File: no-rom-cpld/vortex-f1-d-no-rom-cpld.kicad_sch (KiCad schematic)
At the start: 50 parts, among them J1 JTAG, J2 CONFIG, U1 FDC 9229, U2 XC9572XL, U3 AZ1117-3.3, U4 uPD765AC, U5 74LS06N, U6 74LS06N, U7 SN74LS07N, X1 8Mhz

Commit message: cpl wip
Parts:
- removed C5, C6, C7, C8, C9: 100n, Capacitor_SMD:C_0603_1608Metric_Pad1.08x0.95mm_HandSolder, symbol Device:C_Small
- removed J2: CONFIG, Connector_PinHeader_2.54mm:PinHeader_2x04_P2.54mm_Vertical, symbol Connector_Generic:Conn_02x04_Odd_Even
- removed LED1: LED1, LED_SMD:LED_0805_2012Metric_Pad1.15x1.40mm_HandSolder, symbol Device:LED_Small_Filled
- removed LED2: LED2, LED_SMD:LED_0805_2012Metric_Pad1.15x1.40mm_HandSolder, symbol Device:LED_Small_Filled
- removed LED3: LED3, LED_SMD:LED_0805_2012Metric_Pad1.15x1.40mm_HandSolder, symbol Device:LED_Small_Filled
- removed LED4: LED4, LED_SMD:LED_0805_2012Metric_Pad1.15x1.40mm_HandSolder, symbol Device:LED_Small_Filled
- removed R10, R11, R12, R13, R14, R15, R8, R9: 10k, Resistor_SMD:R_0603_1608Metric_Pad0.98x0.95mm_HandSolder, symbol Device:R_Small
- removed R16, R17, R18, R19, R20, R21, R22, R23: 680, Resistor_SMD:R_0603_1608Metric_Pad0.98x0.95mm_HandSolder, symbol Device:R_Small
- removed R6, R7: 1k, Resistor_SMD:R_0603_1608Metric_Pad0.98x0.95mm_HandSolder, symbol Device:R_Small
- removed U1: FDC 9229, Package_DIP:DIP-20_W7.62mm_Socket, symbol Interface:FDC_9229
- removed U2: XC9572XL, Package_QFP:TQFP-64_10x10mm_P0.5mm, symbol CPLD_Xilinx:XC9572XL-VQ64
- removed U4: uPD765AC, Package_DIP:DIP-40_W15.24mm_Socket, symbol Interface:uPD765AC
- removed U5, U6: 74LS06N, Package_SO:SOIC-14_3.9x8.7mm_P1.27mm, symbol 74xx:74LS06N
- removed U7: SN74LS07N, Package_SO:SOIC-14_3.9x8.7mm_P1.27mm, symbol 74xx:SN74LS07N
- added U1: 37C65, Package_LCC:PLCC-44, symbol Interface:WD37C65-PLCC
- added U2: XC9572XL-VQ44, Package_QFP:TQFP-44_10x10mm_P0.8mm, symbol CPLD_Xilinx:XC9572XL-VQ44
- R1, R2, R3, R4: value 180 -> 150
- R5: value 1k -> 150
- X1: value 8Mhz -> 16Mhz
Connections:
- net LED1 is gone; now on net +5V: R1.1
- net LED2 is gone; now on net +5V: R2.1
- net LED3 is gone; now on net +5V: R3.1
- net LED4 is gone; now on net +5V: R4.1
- net +3.3V: now also C10.1, U2.15 (VCC), U2.26 (VCCIO), U2.35 (VCC)
- net +5V: now also R5.1, U1.24 (DRV), U1.27 (PCVAL), U1.44 (VCC), U1.5 (~{DACK}); no longer C10.1, R5.2
- net A0: now also U1.4 (A0), U2.1 (P0/GCK3)
- net A1: now also U2.2 (P1)
- net A10: now also U2.16 (P10)
- net A11: now also U2.18 (P11)
- net A12: now also U2.19 (P12)
- net A13: now also U2.20 (P13)
- net A14: now also U2.21 (P14)
- net A15: now also U2.22 (P15)
- net A2: now also U2.3 (P2)
- net A3: now also U2.5 (P3)
- net A4: now also U2.6 (P4)
- net A5: now also U2.7 (P5)
- net A6: now also U2.8 (P6)
- net A7: now also U2.12 (P7)
- net A8: now also U2.13 (P8)
- net A9: now also U2.14 (P9)
- net CLK4: now also U2.43 (P32/GCK1)
- net D0: now also U1.7 (DB0), U2.38 (P27)
- net D1: now also U1.8 (DB1)
- net D2: now also U1.9 (DB2)
- net D3: now also U1.10 (DB3)
- net D4: now also U1.11 (DB4)
- net D5: now also U1.12 (DB5)
- net D6: now also U1.13 (DB6)
- net D7: now also U1.14 (DB7)
- net GND: now also U1.34 (GND), U1.6 (TC), U2.17 (GND), U2.25 (GND), U2.4 (GND)
- net RDATA: now also R2.2, S2.30 (Pin_30), U1.21 (~{RDD}); no longer S2.6 (Pin_6)
- net RESET: now also U1.20 (RST), U2.32 (P22)
- net TCK: now also U2.11 (TCK)
- net TDI: now also U2.9 (TDI)
- net TDO: now also U2.24 (TDO)
- net TMS: now also U2.10 (TMS)
- net WDATA: now also S2.22 (Pin_22), U1.30 (~{WD}); no longer S2.14 (Pin_14)
- net ~{CLKIN}: now also U1.26 (XT1)
- net ~{DIR}: now also U1.31 (~{DIRC})
- net ~{DS0}: now also S2.10 (Pin_10), U1.33 (~{DS1}); no longer S2.26 (Pin_26)
- net ~{DS1}: now also S2.12 (Pin_12), U1.35 (~{DS2}); no longer S2.24 (Pin_24)
- net ~{DS2}: now also S2.14 (Pin_14), U1.36 (~{DS3}/~{MO1}); no longer S2.22 (Pin_22)
- net ~{DS3}: now also S2.6 (Pin_6), U1.37 (~{DS4}/~{MO2}); no longer S2.30 (Pin_30)
- net ~{FDCCS}: now also U1.3 (~{CS}), U2.33 (P23/GSR)
- net ~{INDEX}: now also R5.2, S2.8 (Pin_8), U1.43 (~{IDX}); no longer S2.28 (Pin_28)
- net ~{IORD}: now also U1.1 (~{RD}), U2.30 (P20)
- net ~{IORQ}: now also U2.40 (P29)
- net ~{IOWR}: now also U1.2 (~{WR}), U2.31 (P21)
- net ~{MTRON}: now also S2.16 (Pin_16), U2.29 (P19); no longer S2.20 (Pin_20)
- net ~{RDY}: now also R1.2, S2.34 (Pin_34), U1.40 (~{DCHG}); no longer S2.2 (Pin_2)
- net ~{RD}: now also U2.42 (P31)
- net ~{RSET}: now also U2.44 (P33/GCK2)
- net ~{SIDE1}: now also S2.32 (Pin_32), U1.28 (~{HS}); no longer S2.4 (Pin_4)
- net ~{STEP}: now also S2.20 (Pin_20), U1.32 (~{STEP}); no longer S2.16 (Pin_16)
- net ~{TRK00}: now also R4.2, S2.26 (Pin_26), U1.42 (~{TR00}); no longer S2.10 (Pin_10)
- net ~{WGATE}: now also S2.24 (Pin_24), U1.29 (~{WE}); no longer S2.12 (Pin_12)
- net ~{WPT}: now also R3.2, S2.28 (Pin_28), U1.41 (~{WP}); no longer S2.8 (Pin_8)
- net ~{WR}: now also U2.41 (P30)
- new net ~{LDCR}: U1.19 (~{LDCR}), U2.27 (P17)
- new net ~{LDOR}: U1.18 (~{LDOR}), U2.28 (P18)
- no-connect marks 13 -> 36
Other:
- moved on the sheet: C1, C10, C11, C2, J1, S1, S2, U3, X1

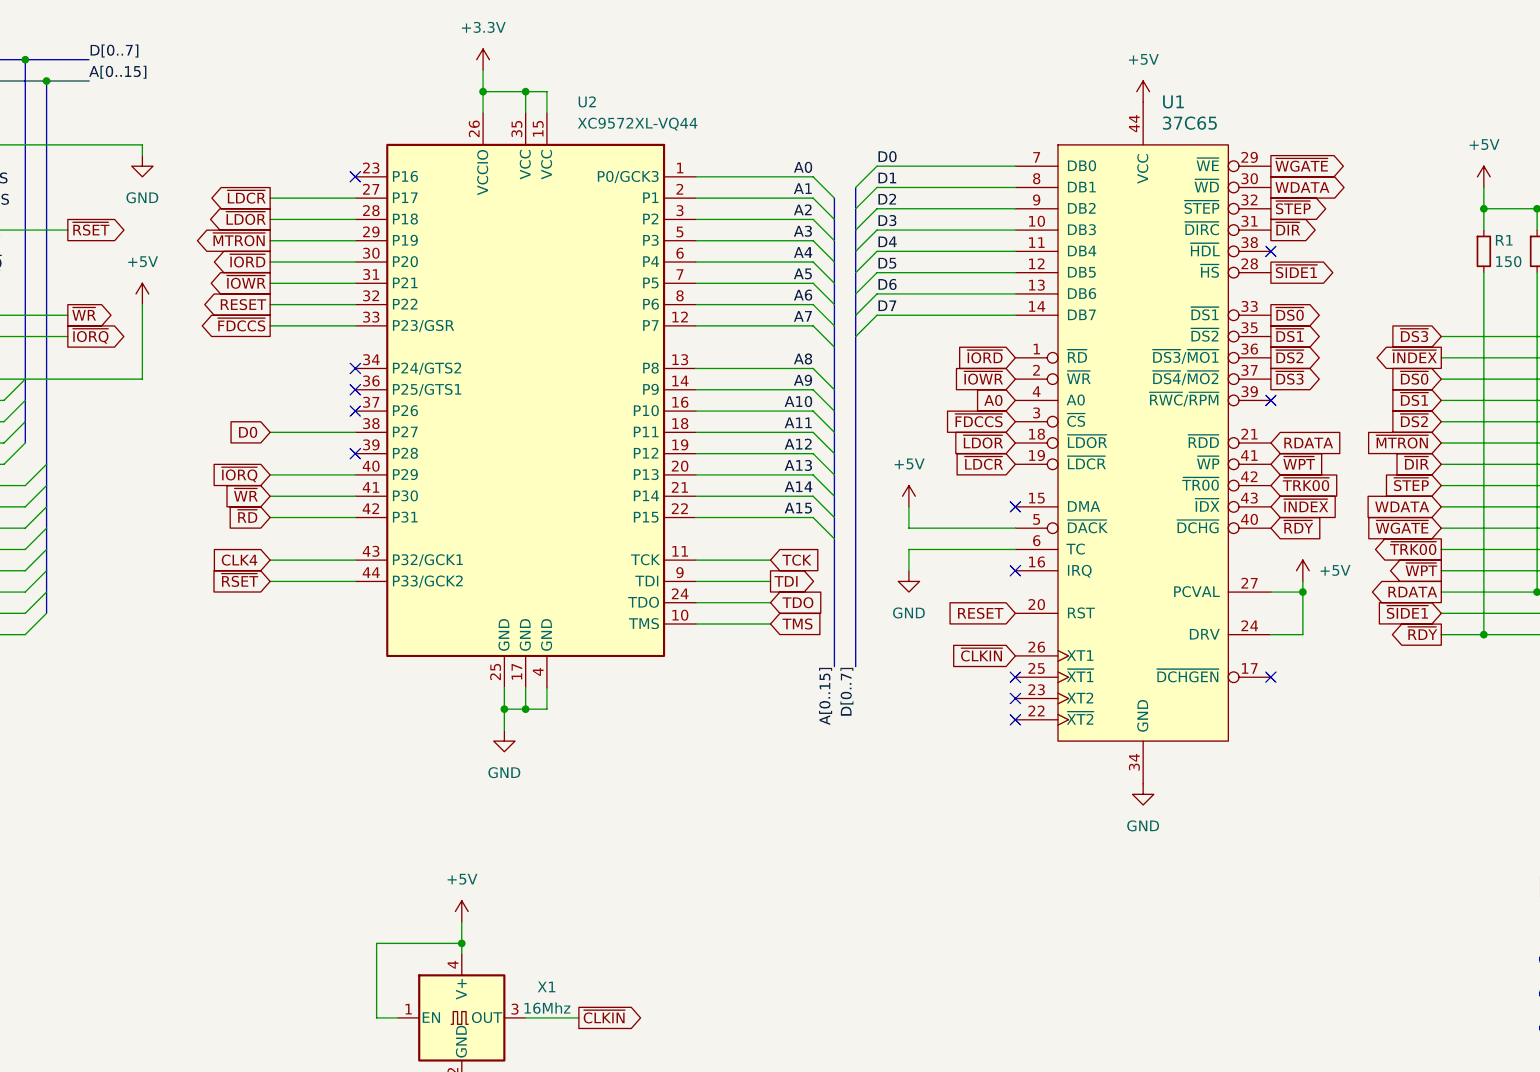
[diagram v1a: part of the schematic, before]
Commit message: add address select jumper to schematics
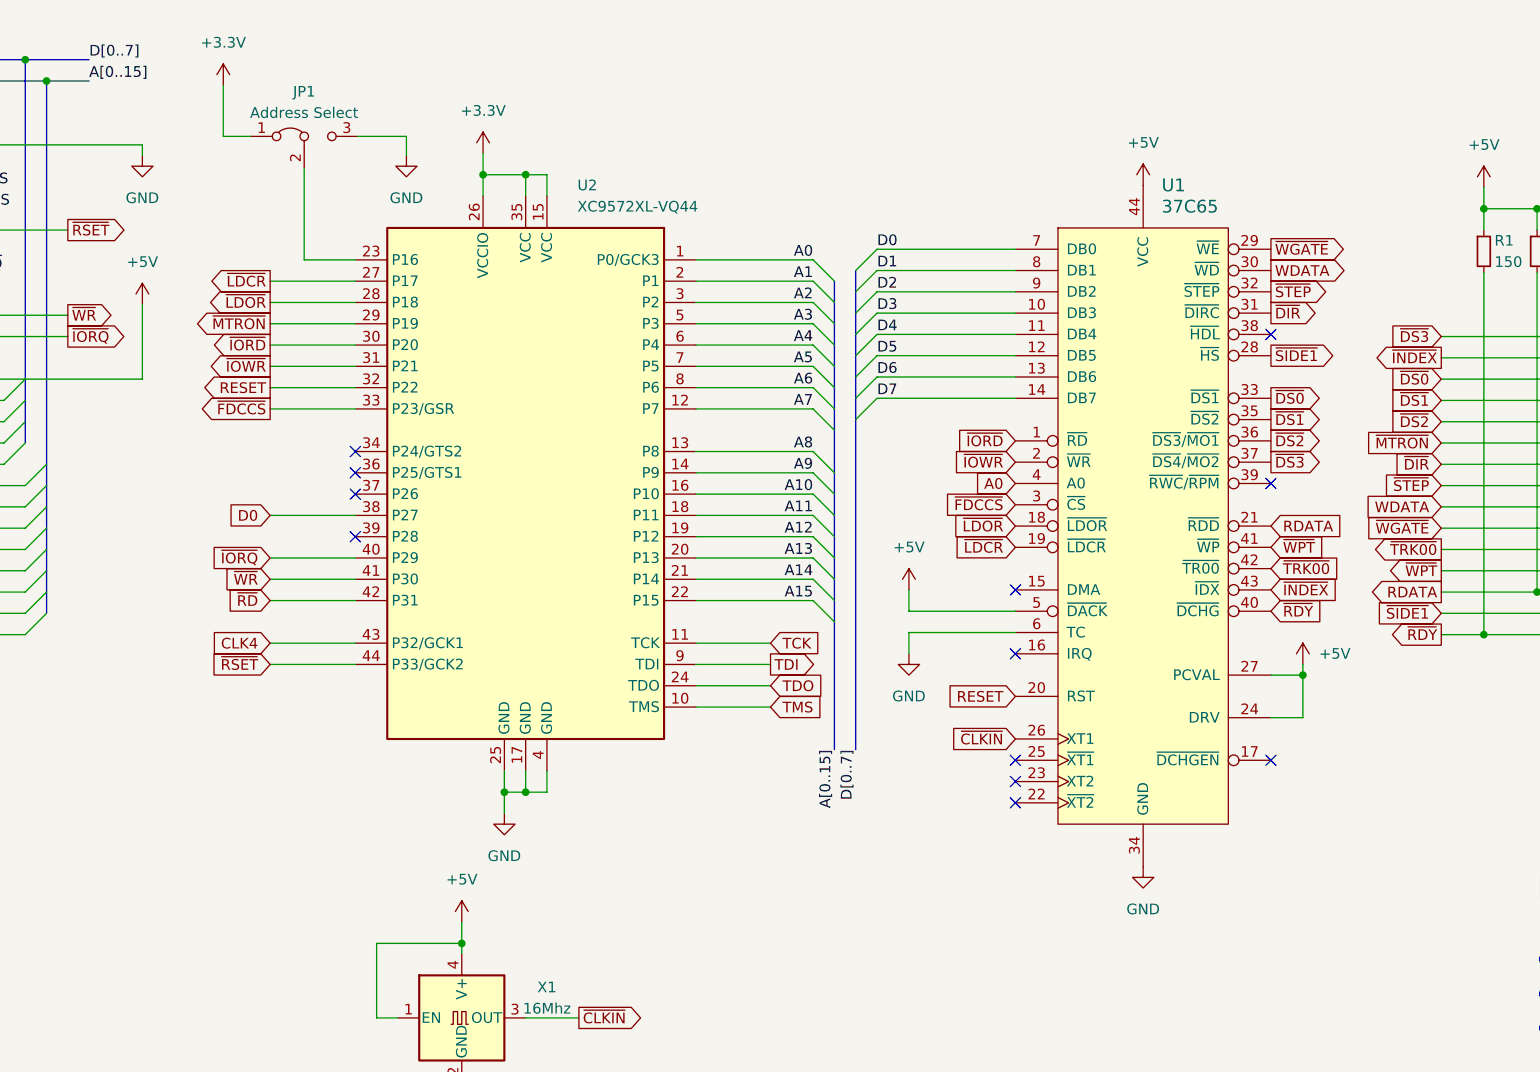
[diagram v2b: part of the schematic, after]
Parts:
- added JP1: Address Select, symbol Jumper:Jumper_3_Bridged12
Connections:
- net +3.3V: now also JP1.1 (A)
- net GND: now also JP1.3 (B)
- net at U2.23 (P16): now also JP1.2 (C)
- no-connect marks 36 -> 35
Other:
- moved on the sheet: U1, U2
